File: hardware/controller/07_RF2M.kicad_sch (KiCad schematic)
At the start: 18 parts, among them J5 RF2M keyed controller link, U50 TPS22918DBVR, U51 SN74LVC244APWR, U52 SN74LVC125APWR

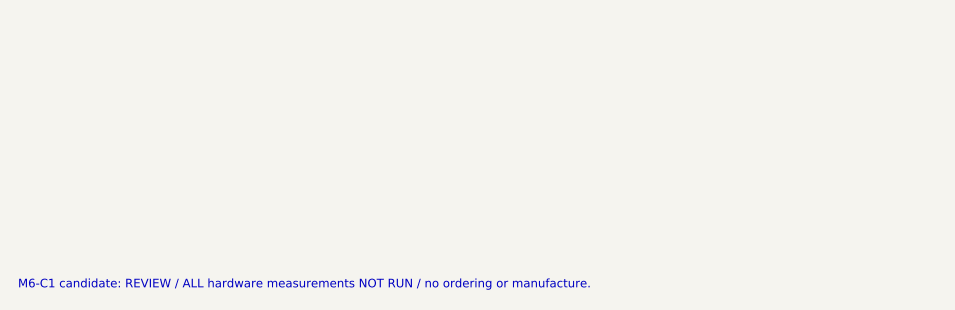
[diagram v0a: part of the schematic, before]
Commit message: M6-C1R1: protect pack identity input and review USB ESD topology
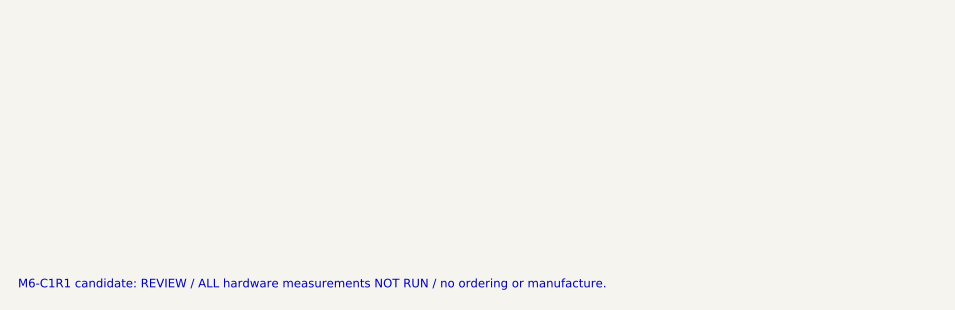
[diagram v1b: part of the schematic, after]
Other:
- note added: "M6-C1R1 candidate: REVIEW / ALL hardware measurements NOT RUN / no ordering or manufacture."
- note removed: "M6-C1 candidate: REVIEW / ALL hardware measurements NOT RUN / no ordering or manufacture."
